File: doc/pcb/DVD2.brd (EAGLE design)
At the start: 48.1 x 42.5 mm, 40 parts, among them IC1 TEENSY_3.1_BASIC_DVD_BP, IC2 74HC14N, IC3 7805, IC4 POLOLU_TB6612FNG

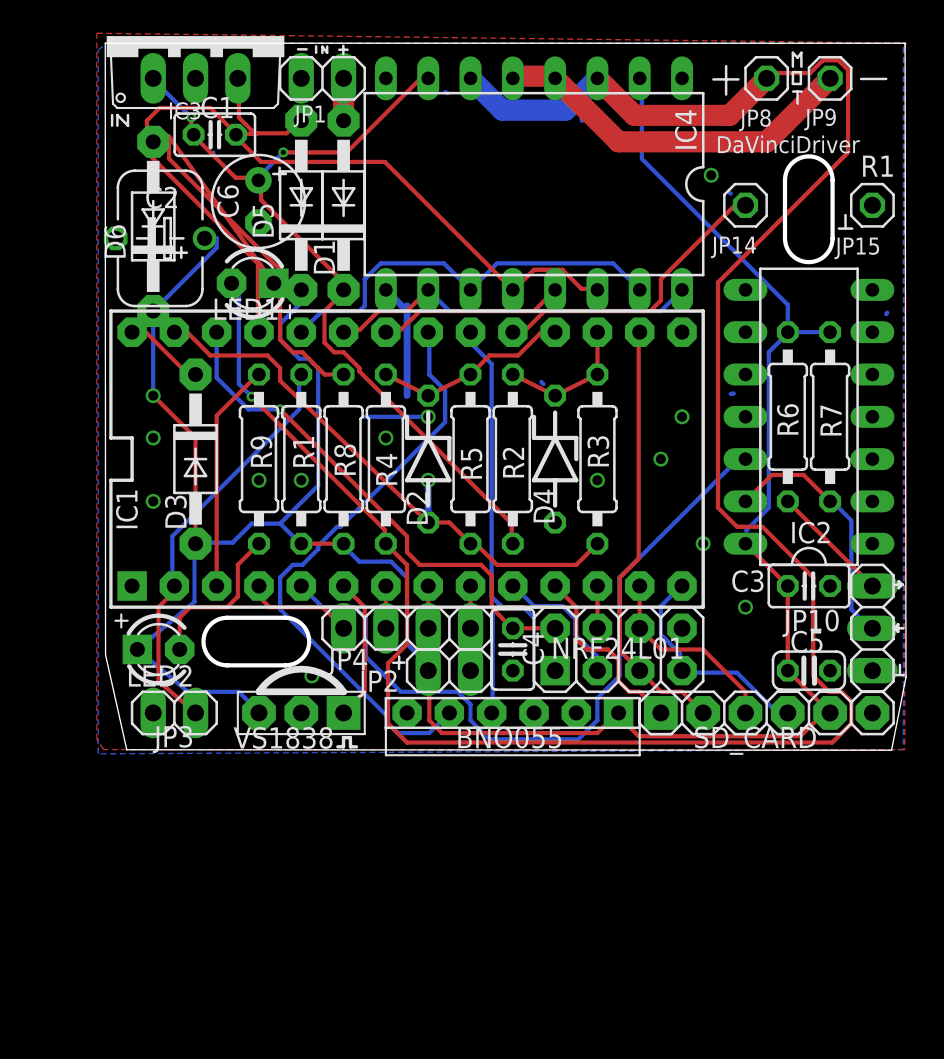
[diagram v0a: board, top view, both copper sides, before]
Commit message: Updated DVD2 with extra Diode(s)
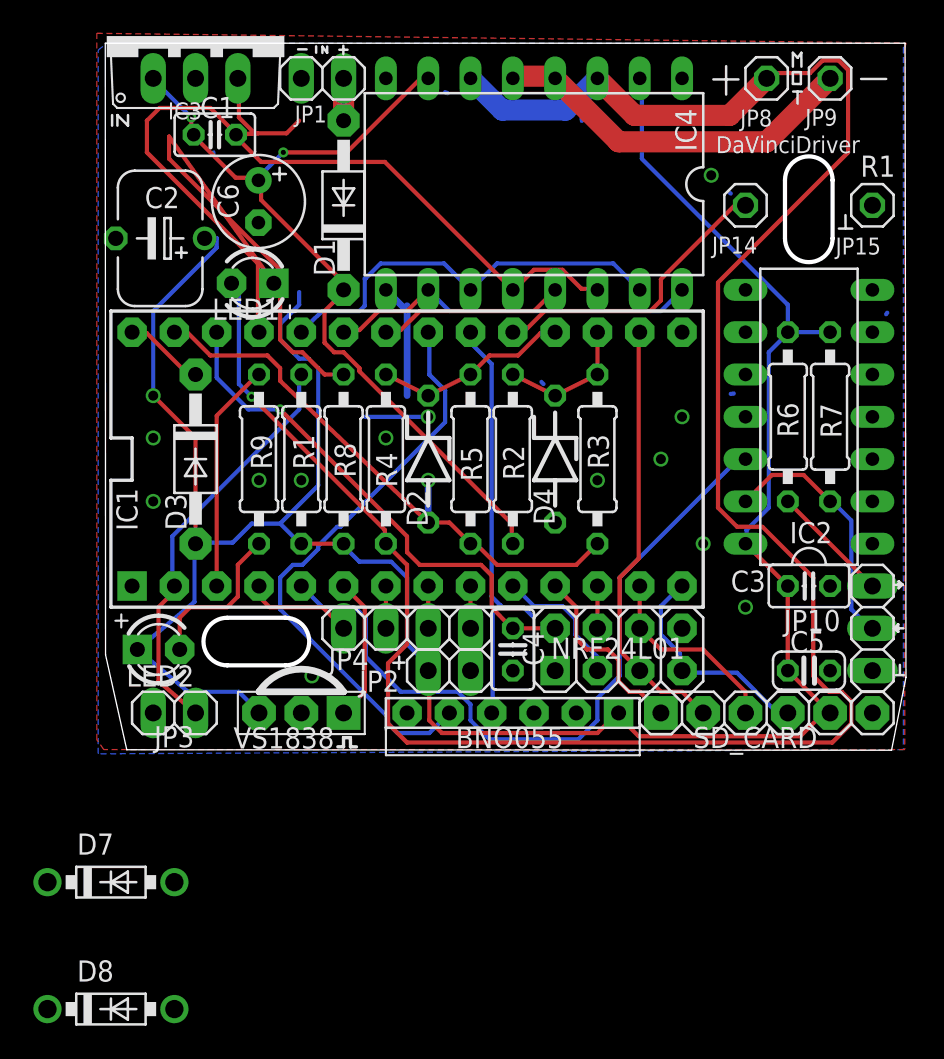
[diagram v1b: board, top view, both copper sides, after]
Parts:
- removed D5, D6: 1N4004, adafruit:DO41-10
- added D7, D8: 1N5817-B, diode:DO41-7.6
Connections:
- net +5V: now also D7.C; no longer D5.C
- net GND: now also D8.C; no longer D6.C
- net N$5: now also D7.A; no longer D5.A
- net N$8: now also D8.A; no longer D6.A
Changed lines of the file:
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@@
 <?xml version="1.0" encoding="utf-8"?>
 <!DOCTYPE eagle SYSTEM "eagle.dtd">
-<eagle version="7.3.0">
+<eagle version="7.5.0">
 <drawing>
 <settings>
@@
 <attribute name="VALUE" x="22.86" y="1.905" size="1.27" layer="27"/>
 </element>
-<element name="D5" library="adafruit" package="DO41-10" value="1N4004" x="16.51" y="33.02" rot="R90"/>
-<element name="D6" library="adafruit" package="DO41-10" value="1N4004" x="7.62" y="31.75" rot="R90"/>
+<element name="D7" library="diode" package="DO41-7.6" value="1N5817-B" x="5.08" y="-7.62"/>
+<element name="D8" library="diode" package="DO41-7.6" value="1N5817-B" x="5.08" y="-15.24"/>
 </elements>
 <signals>
@@
 <wire x1="51.6255" y1="26.4795" x2="51.692809375" y2="26.568396875" width="0.254" layer="16"/>
 <wire x1="42.291" y1="33.7185" x2="42.186728125" y2="33.822775" width="0.254" layer="16"/>
-<contactref element="D6" pad="C"/>
-<wire x1="7.62" y1="2.54" x2="7.62" y2="26.67" width="0" layer="19" extent="1-1"/>
-<wire x1="6.35" y1="10.16" x2="7.62" y2="2.54" width="0" layer="19" extent="1-1"/>
-<wire x1="13.97" y1="16.51" x2="7.62" y2="15.24" width="0" layer="19" extent="1-1"/>
-<wire x1="20.32" y1="20.32" x2="16.51" y2="16.51" width="0" layer="19" extent="16-16"/>
-<wire x1="50.8" y1="12.7" x2="48.26" y2="10.16" width="0" layer="19" extent="1-1"/>
+<contactref element="D8" pad="C"/>
+<wire x1="50.8" y1="27.94" x2="50.8" y2="33.02" width="0" layer="19" extent="1-1"/>
+<wire x1="51.692809375" y1="26.568396875" x2="50.8" y2="27.94" width="0" layer="19" extent="16-16"/>
+<wire x1="50.8" y1="22.86" x2="51.6255" y2="26.4795" width="0" layer="19" extent="16-16"/>
+<wire x1="50.8" y1="17.78" x2="50.8" y2="22.86" width="0" layer="19" extent="1-1"/>
+<wire x1="50.8635" y1="12.7635" x2="50.8" y2="17.78" width="0" layer="19" extent="1-1"/>
+<wire x1="48.26" y1="10.16" x2="50.8" y2="12.7" width="0" layer="19" extent="1-1"/>
+<wire x1="48.26" y1="5.08" x2="48.26" y2="10.16" width="0" layer="19" extent="1-1"/>
+<wire x1="50.8" y1="5.08" x2="48.26" y2="5.08" width="0" layer="19" extent="1-1"/>
+<wire x1="50.8" y1="2.54" x2="50.8" y2="5.08" width="0" layer="19" extent="1-1"/>
+<wire x1="43.18" y1="8.89" x2="48.26" y2="10.16" width="0" layer="19" extent="1-1"/>
+<wire x1="40.64" y1="12.7" x2="43.18" y2="8.89" width="0" layer="19" extent="1-1"/>
+<wire x1="38.1" y1="17.78" x2="40.64" y2="12.7" width="0" layer="19" extent="1-1"/>
+<wire x1="39.37" y1="20.32" x2="38.1" y2="17.78" width="0" layer="19" extent="1-1"/>
+<wire x1="42.2871875" y1="21.6916" x2="39.37" y2="20.32" width="0" layer="19" extent="16-16"/>
+<wire x1="43.18" y1="20.32" x2="42.4815" y2="21.717" width="0" layer="19" extent="16-16"/>
+<wire x1="43.18" y1="25.4" x2="42.4815" y2="21.717" width="0" layer="19" extent="16-16"/>
+<wire x1="34.29" y1="16.51" x2="38.1" y2="17.78" width="0" layer="19" extent="1-1"/>
+<wire x1="31.75" y1="13.97" x2="34.29" y2="16.51" width="0" layer="19" extent="1-1"/>
+<wire x1="31.0515" y1="22.2885" x2="34.29" y2="16.51" width="0" layer="19" extent="16-16"/>
+<wire x1="24.13" y1="20.32" x2="30.92381875" y2="22.416184375" width="0" layer="19" extent="16-16"/>
+<wire x1="22.86" y1="21.59" x2="24.13" y2="20.32" width="0" layer="19" extent="16-16"/>
+<wire x1="21.59" y1="19.05" x2="20.32" y2="20.32" width="0" layer="19" extent="16-16"/>
+<wire x1="24.13" y1="16.51" x2="21.59" y2="19.05" width="0" layer="19" extent="1-1"/>
+<wire x1="16.51" y1="16.51" x2="20.32" y2="20.32" width="0" layer="19" extent="16-16"/>
+<wire x1="13.97" y1="16.51" x2="16.51" y2="16.51" width="0" layer="19" extent="1-1"/>
+<wire x1="7.62" y1="15.24" x2="13.97" y2="16.51" width="0" layer="19" extent="1-1"/>
+<wire x1="7.62" y1="19.05" x2="7.62" y2="15.24" width="0" layer="19" extent="1-1"/>
+<wire x1="6.35" y1="10.16" x2="7.62" y2="15.24" width="0" layer="19" extent="1-1"/>
+<wire x1="7.62" y1="2.54" x2="6.35" y2="10.16" width="0" layer="19" extent="1-1"/>
+<wire x1="42.291" y1="33.7185" x2="43.18" y2="25.4" width="0" layer="19" extent="16-16"/>
+<wire x1="41.1220625" y1="34.82151875" x2="42.186728125" y2="33.822775" width="0" layer="19" extent="16-16"/>
+<wire x1="39.37" y1="40.64" x2="41.1220625" y2="34.82151875" width="0" layer="19" extent="1-1"/>
+<wire x1="33.3375" y1="38.2905" x2="39.37" y2="40.64" width="0" layer="19" extent="16-16"/>
+<wire x1="25.298396875" y1="39.7471875" x2="33.3375" y2="38.2905" width="0" layer="19" extent="16-16"/>
+<wire x1="21.59" y1="40.64" x2="25.146" y2="39.8145" width="0" layer="19" extent="16-16"/>
+<wire x1="16.51" y1="40.64" x2="21.59" y2="40.64" width="0" layer="19" extent="1-1"/>
+<wire x1="11.2395" y1="36.195" x2="16.51" y2="40.64" width="0" layer="19" extent="16-16"/>
+<wire x1="10.048303125" y1="37.256915625" x2="11.2395" y2="36.195" width="0" layer="19" extent="16-16"/>
+<wire x1="13.935884375" y1="31.977603125" x2="11.2395" y2="36.139315625" width="0" layer="19" extent="16-16"/>
+<wire x1="12.32165625" y1="28.337740625" x2="13.935884375" y2="31.977603125" width="0" layer="19" extent="1-1"/>
+<wire x1="5.3701125" y1="31.033521875" x2="12.32165625" y2="28.337740625" width="0" layer="19" extent="1-1"/>
 <wire x1="31.75" y1="5.08" x2="31.75" y2="13.97" width="0" layer="19" extent="1-1"/>
+<wire x1="29.21" y1="5.08" x2="31.75" y2="5.08" width="0" layer="19" extent="1-1"/>
+<wire x1="26.67" y1="5.08" x2="29.21" y2="5.08" width="0" layer="19" extent="1-1"/>
+<wire x1="30.48" y1="2.54" x2="31.75" y2="5.08" width="0" layer="19" extent="1-1"/>
 <wire x1="16.51" y1="2.54" x2="7.62" y2="2.54" width="0" layer="19" extent="1-1"/>
+<wire x1="17.145" y1="4.7625" x2="16.51" y2="2.54" width="0" layer="19" extent="1-1"/>
+<wire x1="1.27" y1="-15.24" x2="7.62" y2="2.54" width="0" layer="19" extent="1-1"/>
 </signal>
 <signal name="+5V">
@@
 <wire x1="9.7155" y1="3.81" x2="6.6675" y2="6.35" width="0.254" layer="16"/>
 <contactref element="JP2" pad="1"/>
-<contactref element="D5" pad="C"/>
 <wire x1="11.43" y1="30.48" x2="11.43" y2="31.0515" width="0.254" layer="16"/>
 <wire x1="7.62" y1="26.67" x2="11.43" y2="30.48" width="0.254" layer="16"/>
@@
 <wire x1="17.526" y1="16.1925" x2="17.526" y2="23.241" width="0.254" layer="16"/>
 <wire x1="15.24" y1="13.9065" x2="17.526" y2="16.1925" width="0.254" layer="16"/>
-<wire x1="16.383" y1="27.813" x2="16.51" y2="27.94" width="0.254" layer="16"/>
 <wire x1="36.7665" y1="1.143" x2="35.6235" y2="2.286" width="0.254" layer="1"/>
 <wire x1="46.482" y1="1.143" x2="36.7665" y2="1.143" width="0.254" layer="1"/>
@@
 <wire x1="24.1935" y1="4.953" x2="24.13" y2="5.08" width="0.254" layer="1"/>
 <wire x1="35.433" y1="2.4765" x2="35.56" y2="2.54" width="0.254" layer="1"/>
+<contactref element="D7" pad="C"/>
+<wire x1="1.27" y1="-7.62" x2="9.7155" y2="3.81" width="0" layer="19" extent="16-16"/>
 </signal>
 <signal name="D4_IR">
@@
 <contactref element="IC3" pad="3"/>
 <contactref element="C1" pad="1"/>
-<contactref element="D5" pad="A"/>
 <wire x1="15.621" y1="37.338" x2="13.9065" y2="37.338" width="0.254" layer="1"/>
 <wire x1="16.383" y1="38.1" x2="15.621" y2="37.338" width="0.254" layer="1"/>
 <wire x1="13.9065" y1="37.338" x2="12.588303125" y2="37.256915625" width="0.254" layer="1"/>
-<wire x1="16.383" y1="38.1" x2="16.51" y2="38.1" width="0.254" layer="1"/>
 <wire x1="12.7635" y1="38.2905" x2="12.7635" y2="40.5765" width="0.254" layer="1"/>
 <wire x1="13.716" y1="37.338" x2="12.7635" y2="38.2905" width="0.254" layer="1"/>
 <wire x1="12.7635" y1="40.5765" x2="12.7" y2="40.64" width="0.254" layer="1"/>
 <wire x1="13.716" y1="37.338" x2="12.588303125" y2="37.256915625" width="0.254" layer="1"/>
+<contactref element="D7" pad="A"/>
+<wire x1="8.89" y1="-7.62" x2="12.588303125" y2="37.256915625" width="0" layer="19" extent="1-1"/>
 </signal>
 <signal name="N$8">
 <contactref element="IC3" pad="2"/>
-<contactref element="D6" pad="A"/>
-<wire x1="7.62" y1="36.83" x2="10.16" y2="40.64" width="0" layer="19" extent="1-1"/>
+<contactref element="D8" pad="A"/>
+<wire x1="8.89" y1="-15.24" x2="10.16" y2="40.64" width="0" layer="19" extent="1-1"/>
 </signal>
 </signals>
